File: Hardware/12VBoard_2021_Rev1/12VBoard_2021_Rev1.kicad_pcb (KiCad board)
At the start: 2 copper layers, 101.6 x 101.6 mm, 170 parts, among them Q1 CSD18537NQ5A, Q10 IRLML2060, Q11 IRLML2060, Q12 IRLML2060, Q13 IRLML2060, Q2 CSD18531Q5A, Q3 IRLML2060, Q4 CSD18537NQ5A, Q5 CSD18531Q5A, Q6 CSD18537NQ5A, Q7 CSD18531Q5A, Q8 IRLML2060, Q9 IRLML2060, U1 LT1910, U10 LM5116, U11 INA198, U12 LM5116, U13 INA198, U14 LT1910, U15 LT1910, U16 LT1910, U17 LT1910, U2 INA198, U3 LT1910, U4 LM2576S-12/NOPB, U5 LT1910, U6 LM2576S-12/NOPB, U7 LM5116, U8 INA198, U9 OKI

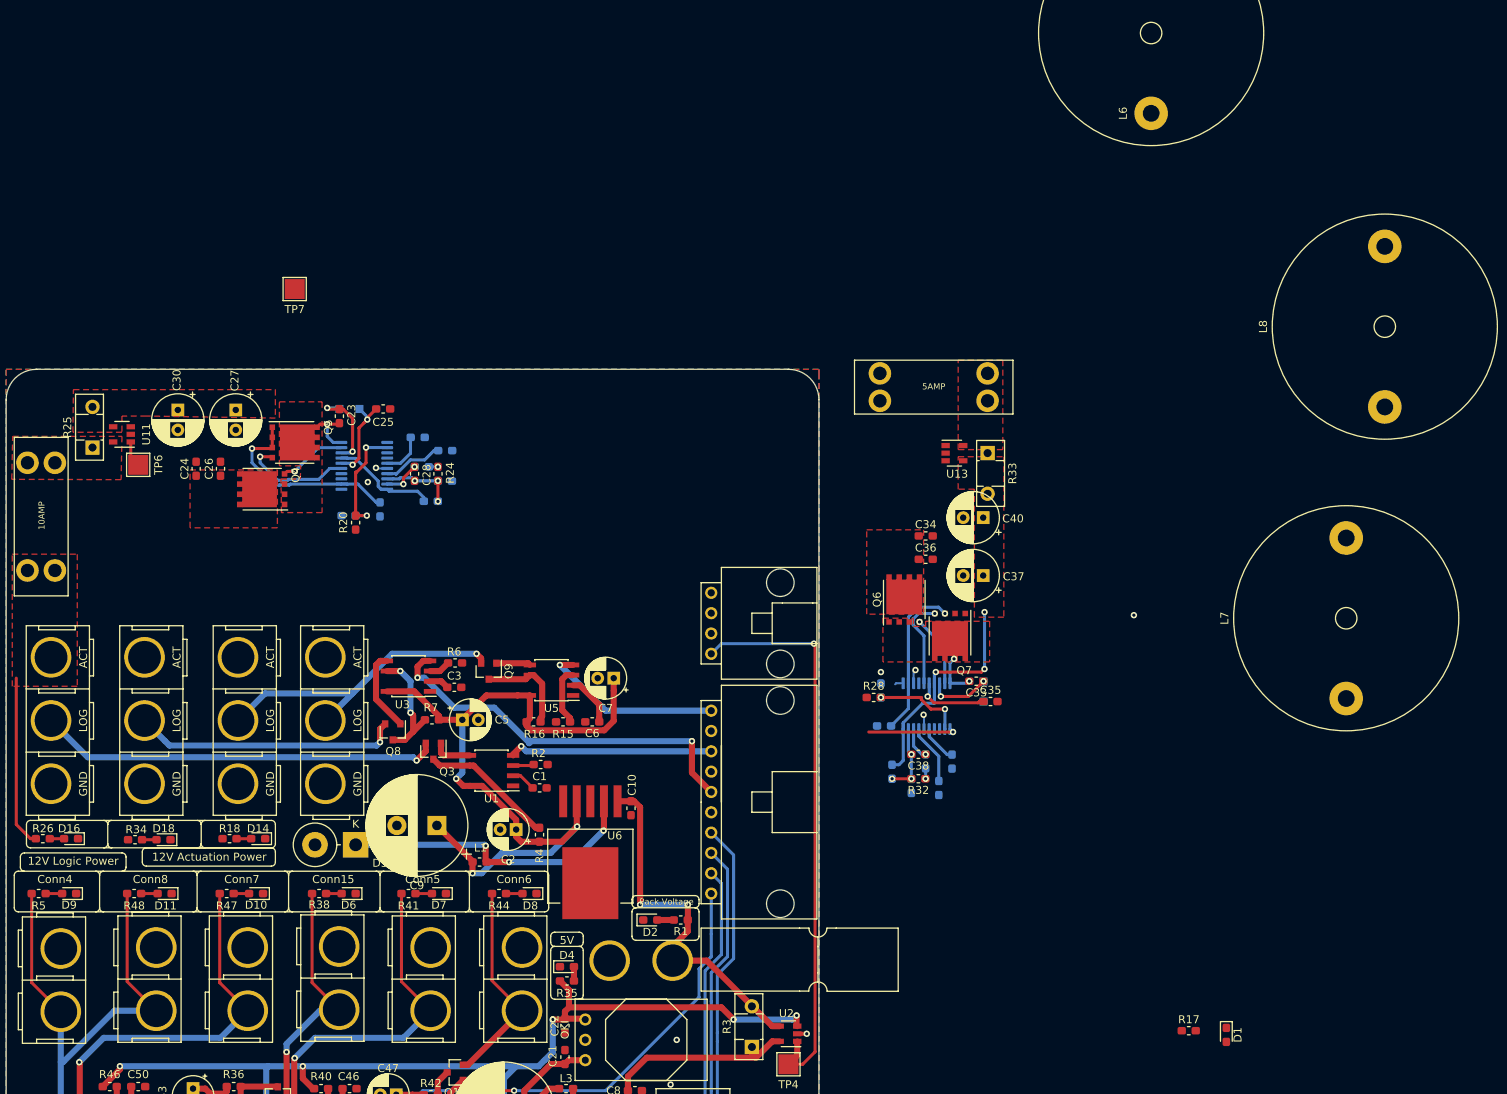
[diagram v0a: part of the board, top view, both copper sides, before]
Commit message: Rearanged logic bick for high current
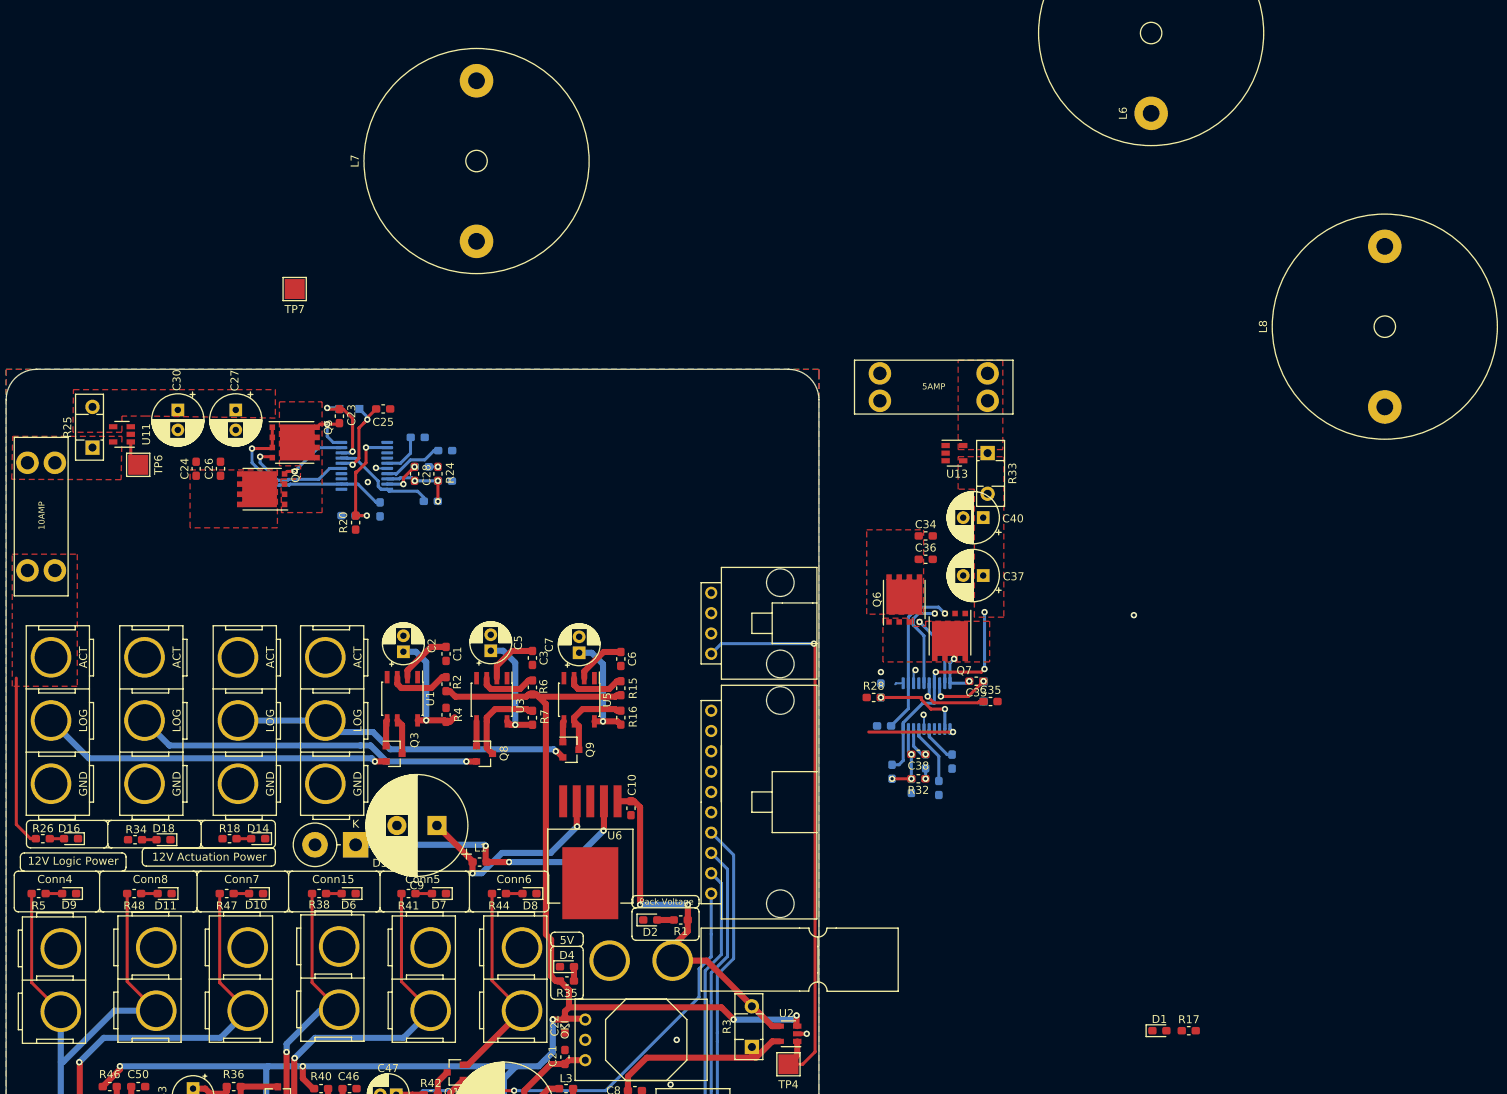
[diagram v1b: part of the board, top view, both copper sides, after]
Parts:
- moved L7 122.8 mm to (174.4, 22.4)
- moved C2 26.3 mm to (165.2, 73.7), turned to 90 degrees
- moved C1 20.4 mm to (170.6, 73.9), turned to 270 degrees
- moved R4 19.0 mm to (170.6, 81.5)
- moved R2 15.5 mm to (170.6, 77.7), turned to 270 degrees
- moved U1 14.3 mm to (165.1, 79.5), turned to 270 degrees
- moved Q9 14.2 mm to (186.2, 85.9), turned to 0 degrees
- moved R7 12.6 mm to (181.4, 81.9), turned to 90 degrees
- moved Q8 11.8 mm to (175.4, 86.4), turned to 0 degrees
- moved R16 10.9 mm to (192.4, 81.9), turned to 90 degrees
- moved U3 10.8 mm to (176.3, 79.7), turned to 270 degrees
- moved C3 10.4 mm to (181.4, 74.4), turned to 270 degrees
- moved R6 10.1 mm to (181.4, 78.1), turned to 270 degrees
- moved C5 9.34 mm to (176.1, 73.5), turned to 90 degrees
- moved C6 8.63 mm to (192.4, 74.6), turned to 270 degrees
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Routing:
- net +5V: track 134.8 -> 194.6 mm
- net /High Current Outputs/GimbalCTL_Log: track 48.5 -> 0.00 mm, vias 2 -> 0
- net /High Current Outputs/AuxMountCTL_Log: track 25.6 -> 0.00 mm, vias 1 -> 0
- net /High Current Outputs/12VLogic/12VLogic: track 97.5 -> 72.2 mm, vias 3 -> 5
- net /High Current Outputs/MultiMediaCTL_Log: track 22.9 -> 0.00 mm, vias 1 -> 0
- net Net-(Q3-Pad3): track 16.8 -> 4.44 mm
- net /High Current Outputs/Gimbal/12VLogicGimbal: track 33.5 -> 43.6 mm
- net Net-(Q8-Pad1): track 10.2 -> 3.11 mm
- net /High Current Outputs/AuxMount/12VLogicAuxMount: track 50.4 -> 44.0 mm
- net Net-(R2-Pad1): track 2.62 -> 7.72 mm
- net Net-(R6-Pad1): track 2.67 -> 7.22 mm
- net Net-(C3-Pad1): track 2.47 -> 6.75 mm
- net Net-(Q8-Pad3): track 15.0 -> 11.1 mm, vias 2 -> 0
- net Net-(C1-Pad1): track 3.07 -> 6.89 mm
- net /High Current Outputs/Multimedia/Extra/12VLogicMultiMedia: track 39.5 -> 43.0 mm
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
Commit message: Extended Board
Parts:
- C24, C26, Q4, Q5, U11: moved to B.Cu
- moved L7 55.3 mm to (139.6, 65.3)
- moved C25 28.7 mm to (191.3, 46.0)
- moved C28 28.7 mm to (195.2, 54.1)
- moved C29 28.7 mm to (196.1, 53.2)
- moved R23 28.7 mm to (199.0, 55.0)
- moved R24 28.7 mm to (198.1, 54.1)
- moved C23 28.7 mm to (185.8, 46.9)
- moved C31 28.7 mm to (195.6, 49.5)
- moved C32 28.7 mm to (199.0, 51.2)
- moved D15 28.7 mm to (187.1, 46.0)
- moved R19 28.7 mm to (190.9, 58.5)
- moved R20 28.7 mm to (187.8, 60.2)
- moved R21 28.7 mm to (186.9, 59.3)
- moved R22 28.7 mm to (197.2, 57.5)
- moved U10 28.7 mm to (188.9, 53.1)
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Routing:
- net /High Current Outputs/12VLogic/12VLogic: track 72.2 -> 107.9 mm
- net CS: track 65.0 -> 48.3 mm, vias 3 -> 2
- net LO: track 37.2 -> 23.2 mm, vias 3 -> 2
- net HO: track 26.3 -> 18.2 mm, vias 3 -> 2
- net SW: track 18.1 -> 12.0 mm, vias 6 -> 5
- net /High Current Outputs/AuxMountSense: track 3.25 -> 0.00 mm
- net HB: track 26.1 -> 22.9 mm, vias 6 -> 5
- net Net-(F2-Pad2): track 0.00 -> 2.52 mm
- net VOUTVCCX: track 49.5 -> 52.0 mm
- added copper zone on B.Cu, net /High Current Outputs/PackVoltage
- added copper zone on B.Cu, net SW
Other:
- board size 101.6 x 101.6 mm -> 101.6 x 129.4 mm

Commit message: I changed stuff
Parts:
- moved C24 25.3 mm to (172.5, 46.7)
- moved C26 25.3 mm to (172.5, 49.8)
- moved Q4 25.3 mm to (175.0, 55.0)
- moved Q5 25.3 mm to (169.2, 59.1)
- moved L7 17.2 mm to (151.4, 52.8), turned to 180 degrees
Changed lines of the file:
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@@
   (page A4)
   (layers
-    (0 F.Cu signal hide)
-    (31 B.Cu signal hide)
+    (0 F.Cu signal)
+    (31 B.Cu signal)
     (32 B.Adhes user)
     (33 F.Adhes user)
@@
   )
   (module Inductor_THT:L_Radial_D27.9mm_P20.07mm_Vishay_IHB-3 (layer F.Cu)
-    (at 139.573 65.278 90)
+    (at 151.384 52.832 180)
     (descr "Inductor, Radial series, Radial, pin pitch=20.07mm, , diameter=27.9mm, Vishay, IHB-3, http://www.vishay.com/docs/34015/ihb.pdf")
     (tags "Inductor Radial series Radial pin pitch 20.07mm  diameter 27.9mm Vishay IHB-3")
-    (fp_text reference L7 (at 10.035 -15.2 90) (layer F.SilkS)
+    (fp_text reference L7 (at 10.035 -15.2) (layer F.SilkS)
       (effects (font (size 1 1) (thickness 0.15)))
     )
-    (fp_text value 10uH (at 10.035 15.2 90) (layer F.Fab)
+    (fp_text value 10uH (at 10.035 15.2) (layer F.Fab)
       (effects (font (size 1 1) (thickness 0.15)))
     )
-    (fp_text user %R (at 10.035 0 90) (layer F.Fab)
+    (fp_text user %R (at 10.035 0) (layer F.Fab)
       (effects (font (size 1 1) (thickness 0.15)))
     )
@@
     (fp_line (start 24.24 14.2) (end 24.24 -14.2) (layer F.CrtYd) (width 0.05))
     (fp_line (start 24.24 -14.2) (end -4.17 -14.2) (layer F.CrtYd) (width 0.05))
-    (pad 2 thru_hole circle (at 20.07 0 90) (size 4.2 4.2) (drill 2.1) (layers *.Cu *.Mask)
+    (pad 2 thru_hole circle (at 20.07 0 180) (size 4.2 4.2) (drill 2.1) (layers *.Cu *.Mask)
       (net 5 VOUTVCCX))
-    (pad 1 thru_hole circle (at 0 0 90) (size 4.2 4.2) (drill 2.1) (layers *.Cu *.Mask)
+    (pad 1 thru_hole circle (at 0 0 180) (size 4.2 4.2) (drill 2.1) (layers *.Cu *.Mask)
       (net 23 SW))
     (model ${KISYS3DMOD}/Inductor_THT.3dshapes/L_Radial_D27.9mm_P20.07mm_Vishay_IHB-3.wrl
@@
   )
   (module Capacitor_SMD:C_0603_1608Metric_Pad1.05x0.95mm_HandSolder (layer B.Cu)
-    (at 147.814 55.372 180)
+    (at 172.452 49.784 180)
     (descr "Capacitor SMD 0603 (1608 Metric), square (rectangular) end terminal, IPC_7351 nominal with elongated pad for handsoldering. (Body size source: http://www.tortai-tech.com/upload/download/2011102023233369053.pdf), generated with kicad-footprint-generator")
     (tags "capacitor handsolder")
@@
   )
   (module Capacitor_SMD:C_0603_1608Metric_Pad1.05x0.95mm_HandSolder (layer B.Cu)
-    (at 147.814 52.324 180)
+    (at 172.452 46.736 180)
     (descr "Capacitor SMD 0603 (1608 Metric), square (rectangular) end terminal, IPC_7351 nominal with elongated pad for handsoldering. (Body size source: http://www.tortai-tech.com/upload/download/2011102023233369053.pdf), generated with kicad-footprint-generator")
     (tags "capacitor handsolder")
@@
   )
   (module Package_SON:VSONP-8-1EP_5x6_P1.27mm (layer B.Cu)
-    (at 150.368 60.579 90)
+    (at 175.006 54.991 90)
     (descr "SON, 8-Leads, Body 5x6x1mm, Pitch 1.27mm; (see Texas Instruments CSD18531Q5A http://www.ti.com/lit/ds/symlink/csd18531q5a.pdf)")
     (tags "VSONP 1.27")
@@
   )
   (module Package_SON:VSONP-8-1EP_5x6_P1.27mm (layer B.Cu)
-    (at 144.526 64.643 270)
+    (at 169.164 59.055 270)
     (descr "SON, 8-Leads, Body 5x6x1mm, Pitch 1.27mm; (see Texas Instruments CSD18531Q5A http://www.ti.com/lit/ds/symlink/csd18531q5a.pdf)")
     (tags "VSONP 1.27")
@@
   (segment (start 352.679 87.376) (end 352.679 84.963) (width 0.381) (layer B.Cu) (net 23))
   (segment (start 352.679 87.376) (end 355.092 87.376) (width 0.381) (layer B.Cu) (net 23))
-  (segment (start 142.24 67.824) (end 142.621 67.443) (width 0.381) (layer B.Cu) (net 23))
+  (segment (start 166.878 62.236) (end 167.259 61.855) (width 0.381) (layer B.Cu) (net 23))
   (via (at 229.743 69.932) (size 0.8) (drill 0.4) (layers F.Cu B.Cu) (net 24))
   (segment (start 232.903 73.092) (end 229.743 69.932) (width 0.381) (layer B.Cu) (net 24))
@@
   (segment (start 352.029 83.252) (end 348.742 79.965) (width 0.381) (layer B.Cu) (net 24))
   (segment (start 352.029 87.376) (end 352.029 83.252) (width 0.381) (layer B.Cu) (net 24))
-  (segment (start 148.1455 63.6965) (end 148.463 63.379) (width 0.381) (layer B.Cu) (net 24))
+  (segment (start 172.7835 58.1085) (end 173.101 57.791) (width 0.381) (layer B.Cu) (net 24))
   (segment (start 188.113 55.365) (end 186.7925 55.365) (width 0.381) (layer B.Cu) (net 25))
   (segment (start 190.406 57.658) (end 188.113 55.365) (width 0.381) (layer B.Cu) (net 25))
@@
   (segment (start 347.479 88.1135) (end 347.479 87.376) (width 0.381) (layer B.Cu) (net 25))
   (segment (start 345.186 92.837) (end 345.186 92.362) (width 0.381) (layer B.Cu) (net 25))
-  (segment (start 142.621 61.843) (end 143.891 61.843) (width 0.381) (layer B.Cu) (net 25))
-  (segment (start 143.891 61.843) (end 145.161 61.843) (width 0.381) (layer B.Cu) (net 25))
+  (segment (start 167.259 56.255) (end 168.529 56.255) (width 0.381) (layer B.Cu) (net 25))
+  (segment (start 168.529 56.255) (end 169.799 56.255) (width 0.381) (layer B.Cu) (net 25))
   (segment (start 229.626058 68.879) (end 231.648 68.879) (width 0.381) (layer B.Cu) (net 26))
   (segment (start 228.952499 69.552559) (end 229.626058 68.879) (width 0.381) (layer B.Cu) (net 26))
@@
     (polygon
       (pts
-        (xy 149.098 65.3415) (xy 147.447 65.405) (xy 147.447 62.738) (xy 136.906 62.738) (xy 136.906 68.072)
-        (xy 153.289 68.072) (xy 153.289 62.992) (xy 149.098 62.9285)
+        (xy 173.736 59.7535) (xy 172.085 59.817) (xy 172.085 57.15) (xy 161.544 57.15) (xy 161.544 62.484)
+        (xy 177.927 62.484) (xy 177.927 57.404) (xy 173.736 57.3405)
       )
     )
@@
     (polygon
       (pts
-        (xy 217.17 38.862) (xy 217.17 139.954) (xy 115.57 139.954) (xy 115.57 38.354) (xy 217.17 38.354)
+        (xy 217.17 38.862) (xy 217.17 139.954) (xy 115.57 139.954) (xy 115.57 10.541) (xy 217.17 10.541)
       )
     )
@@
     (polygon
       (pts
-        (xy 217.17 38.862) (xy 217.17 139.954) (xy 115.57 139.954) (xy 115.57 38.354) (xy 217.17 38.354)
+        (xy 217.17 38.862) (xy 217.17 139.954) (xy 115.57 139.954) (xy 115.57 10.541) (xy 217.17 10.541)
       )
     )
@@
     (polygon
       (pts
-        (xy 147.955 62.484) (xy 155.194 62.484) (xy 155.194 51.562) (xy 147.955 51.562)
+        (xy 172.593 56.896) (xy 179.832 56.896) (xy 179.832 45.974) (xy 172.593 45.974)
       )
     )

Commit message: Started work on updated layout
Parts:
- removed the C14 at (349.4, 69.0)
- removed the C15 at (356.7, 66.7)
- removed the C16 at (355.0, 97.4)
- removed the C18 at (356.7, 73.9)
- removed C19, C31, C41: 470pF, Capacitor_SMD:C_0603_1608Metric_Pad1.05x0.95mm_HandSolder
- removed C20: 33pF, Capacitor_SMD:C_0603_1608Metric_Pad1.05x0.95mm_HandSolder
- removed C23, C26, C33, C36: 100nF, Capacitor_SMD:C_0603_1608Metric_Pad1.05x0.95mm_HandSolder
- removed C24, C34: 2.2uF, Capacitor_SMD:C_0603_1608Metric_Pad1.05x0.95mm_HandSolder
- removed C25, C35: 1uF, Capacitor_SMD:C_0603_1608Metric_Pad1.05x0.95mm_HandSolder
- removed C27, C30, C37, C40: 100uF, Capacitor_THT:CP_Radial_D6.3mm_P2.50mm
- removed C28, C38: 10pF, Capacitor_SMD:C_0603_1608Metric_Pad1.05x0.95mm_HandSolder
- removed C29, C39: 120pF, Capacitor_SMD:C_0603_1608Metric_Pad1.05x0.95mm_HandSolder
- removed C32, C42: 33nF, Capacitor_SMD:C_0603_1608Metric_Pad1.05x0.95mm_HandSolder
- removed the D12 at (356.9, 88.7)
- removed D17: 1.25V 250mA, Diode_SMD:D_SOD-323_HandSoldering
- removed L6, L7, L8: 10uH, Inductor_THT:L_Radial_D27.9mm_P20.07mm_Vishay_IHB-3
- removed Q1, Q4, Q6: CSD18537NQ5A, Package_SON:VSONP-8-1EP_5x6_P1.27mm
- removed Q2, Q5, Q7: CSD18531Q5A, Package_SON:VSONP-8-1EP_5x6_P1.27mm
- removed the R10 at (343.3, 88.5)
- removed R24, R32: 261K, Resistor_SMD:R_0603_1608Metric_Pad1.05x0.95mm_HandSolder
- removed R25: 50m, Package_TO_SOT_THT:TO-126-2_Vertical
- removed R26: 1.2k, Resistor_SMD:R_0603_1608Metric_Pad1.05x0.95mm_HandSolder
- removed R27: 5m, Resistor_SMD:R_0603_1608Metric_Pad1.05x0.95mm_HandSolder
- removed R28: 36.5K, Resistor_SMD:R_0603_1608Metric_Pad1.05x0.95mm_HandSolder
- removed R29: 2.26K, Resistor_SMD:R_0603_1608Metric_Pad1.05x0.95mm_HandSolder
- removed R30: 86.6K, Resistor_SMD:R_0603_1608Metric_Pad1.05x0.95mm_HandSolder
- removed R31: 9.76k, Resistor_SMD:R_0603_1608Metric_Pad1.05x0.95mm_HandSolder
- removed TP6: TestPoint, TestPoint:TestPoint_Pad_2.5x2.5mm
- removed the U10 at (188.9, 53.1)
- removed the U12 at (230.6, 80.5)
- removed the U7 at (349.8, 90.2)
- added C13: 0.1uF, Capacitor_SMD:C_0603_1608Metric_Pad1.05x0.95mm_HandSolder, F.Cu at (252.5, 91.1)
- added C14: 10uF, Capacitor_THT:CP_Radial_D5.0mm_P2.00mm, F.Cu at (257.8, 88.3)
- added C14: 10uF, Capacitor_THT:CP_Radial_D5.0mm_P2.00mm, F.Cu at (349.4, 69.0)
- added C15: 0.1uF, Capacitor_SMD:C_0603_1608Metric_Pad1.05x0.95mm_HandSolder, F.Cu at (283.1, 104.6)
- added C15: 0.1uF, Capacitor_SMD:C_0603_1608Metric_Pad1.05x0.95mm_HandSolder, F.Cu at (356.7, 66.7)
- added C16: 10uF, Capacitor_THT:CP_Radial_D5.0mm_P2.00mm, F.Cu at (283.1, 100.1)
- added C16: 10uF, Capacitor_THT:CP_Radial_D5.0mm_P2.00mm, F.Cu at (354.1, 109.5)
- added C17: 0.1uF, Capacitor_SMD:C_0603_1608Metric_Pad1.05x0.95mm_HandSolder, F.Cu at (289.4, 85.0)
- added C18: 10uF, Capacitor_THT:CP_Radial_D5.0mm_P2.00mm, F.Cu at (289.4, 80.5)
- added C18: 10uF, Capacitor_THT:CP_Radial_D5.0mm_P2.00mm, F.Cu at (356.7, 73.9)
- added D1: Logic Power Green, Diode_SMD:D_0603_1608Metric_Pad1.05x0.95mm_HandSolder, F.Cu at (259.9, 104.9)
- added D12: Aux Mount Acuation Gree, Diode_SMD:D_0603_1608Metric_Pad1.05x0.95mm_HandSolder, F.Cu at (248.1, 91.2)
- added D12: Aux Mount Acuation Gree, Diode_SMD:D_0603_1608Metric_Pad1.05x0.95mm_HandSolder, B.Cu at (362.7, 105.2)
- added D13: Aux Mount Acuation Gree, Diode_SMD:D_0603_1608Metric_Pad1.05x0.95mm_HandSolder, F.Cu at (145.4, -6.75)
- added F4: 5A, MRDT_Passives:ATC_Fuse_Block, F.Cu at (249.6, 79.4)
- added R10: 50m, Package_TO_SOT_THT:TO-126-2_Vertical, F.Cu at (248.1, 87.8)
- added R10: 50m, Package_TO_SOT_THT:TO-126-2_Vertical, B.Cu at (343.3, 116.3)
- added R11: 0.01, Resistor_SMD:R_0603_1608Metric_Pad1.05x0.95mm_HandSolder, F.Cu at (268.8, 89.5)
- added R12: 1.2k, Resistor_SMD:R_0603_1608Metric_Pad1.05x0.95mm_HandSolder, F.Cu at (268.6, 92.0)
- added R13: 5.1K, Resistor_SMD:R_0603_1608Metric_Pad1.05x0.95mm_HandSolder, F.Cu at (278.8, 104.6)
- added R17: 0.01, Resistor_SMD:R_0603_1608Metric_Pad1.05x0.95mm_HandSolder, F.Cu at (274.4, 104.5)
- added R19: 5.1K, Resistor_SMD:R_0603_1608Metric_Pad1.05x0.95mm_HandSolder, F.Cu at (285.0, 85.0)
- added R20: 0.01, Resistor_SMD:R_0603_1608Metric_Pad1.05x0.95mm_HandSolder, F.Cu at (280.7, 84.9)
- added R8: 1.2k, Resistor_SMD:R_0603_1608Metric_Pad1.05x0.95mm_HandSolder, F.Cu at (264.3, 104.8)
- added R9: 5.1K, Resistor_SMD:R_0603_1608Metric_Pad1.05x0.95mm_HandSolder, F.Cu at (264.2, 90.9)
- added TP1: TestPoint, TestPoint:TestPoint_Pad_2.5x2.5mm, F.Cu at (264.3, 87.3)
- added U10: INA198, Package_TO_SOT_SMD:SOT-23-5, F.Cu at (269.3, 86.0)
- added U10: INA198, Package_TO_SOT_SMD:SOT-23-5, B.Cu at (192.5, 65.5)
- added U12: LT1910, Package_SO:SOIC-8-N7_3.9x4.9mm_P1.27mm, F.Cu at (276.5, 100.1)
- added U12: LT1910, Package_SO:SOIC-8-N7_3.9x4.9mm_P1.27mm, B.Cu at (235.7, 98.0)
- added U18: FDS66900AS, Package_SO:SOIC-8_3.9x4.9mm_P1.27mm, F.Cu at (205.3, -47.1)
- added U19: LT1910, Package_SO:SOIC-8-N7_3.9x4.9mm_P1.27mm, F.Cu at (282.8, 80.4)
- added U20: FDS66900AS, Package_SO:SOIC-8_3.9x4.9mm_P1.27mm, F.Cu at (132.5, -4.82)
- added U7: LT1910, Package_SO:SOIC-8-N7_3.9x4.9mm_P1.27mm, F.Cu at (271.1, 80.4)
- added U7: LT1910, Package_SO:SOIC-8-N7_3.9x4.9mm_P1.27mm, B.Cu at (348.0, 109.7)
- added VR1: Q36SR12020NRFA, MRDT_Actives:Q36SR12020NRFA, F.Cu at (160.5, -21.6)
- C10: value 100uF -> 330uF; footprint Capacitor_SMD:C_0603_1608Metric_Pad1.05x0.95mm_HandSolder -> Capacitor_THT:CP_Radial_D8.0mm_P3.50mm
- C11: value 2.2uF -> 330uF; footprint Capacitor_SMD:C_0603_1608Metric_Pad1.05x0.95mm_HandSolder -> Capacitor_THT:CP_Radial_D8.0mm_P3.50mm
- C13: value 1uF -> 0.1uF
- C17: value 120pF -> 0.1uF
- C4, C9: footprint Capacitor_THT:CP_Radial_D12.5mm_P5.00mm -> Capacitor_THT:CP_Radial_D10.0mm_P5.00mm
- D14: value Multimedia Acuation Green -> Multimedia Actuation Green
- D15: value 1.25V 250mA -> Aux Mount Acuation Gree; footprint Diode_SMD:D_SOD-323_HandSoldering -> Diode_SMD:D_0603_1608Metric_Pad1.05x0.95mm_HandSolder
- D16: value AuxMount Acuation Green -> Aux Mount Acuation Gree
- F1: value 10AMP -> 10A
- F2: value 10AMP -> 20
- F3: value 5AMP -> 5A
- R11: value 86.6K -> 0.01
- R12: value 9.76 -> 1.2k
- R13: value 261K -> 5.1K
- R17: value 1.2k -> 0.01
- R19: value 5m -> 5.1K
- R20: value 36.5K -> 0.01
- R21: value 2.26K -> 1.2k
- R22: value 86.6K -> 1.2k
- R23: value 9.76K -> 1.2k
- R8: value 5m -> 1.2k
- R9: value 36.5K -> 5.1K
- U11: value INA198 -> FDS66900AS; footprint Package_TO_SOT_SMD:SOT-23-5 -> Package_SO:SOIC-8_3.9x4.9mm_P1.27mm
- moved C12 162.5 mm to (193.5, 93.2), turned to 270 degrees
- moved C10 76.0 mm to (255.5, 49.0)
- moved TP7 52.2 mm to (114.0, -7.87)
- moved R13 23.8 mm to (365.5, 120.1)
- moved R12 19.8 mm to (369.5, 115.3)
- moved C11 19.2 mm to (368.3, 75.2)
- moved C13 18.3 mm to (365.6, 106.4)
- moved R9 17.0 mm to (341.6, 106.4)
- moved R8 16.6 mm to (338.6, 108.5)
- moved R11 14.6 mm to (363.0, 114.6)
- moved C17 13.7 mm to (361.7, 109.0)
- moved D15 11.9 mm to (178.6, 54.4)
- moved U11 10.4 mm to (130.6, 42.7)
- moved R23 6.49 mm to (199.4, 61.5)
- moved R22 5.93 mm to (195.7, 63.2)
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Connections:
- C1 pad 2: AGNDPGND -> GND
- C10 pad 1: /High Current Outputs/PackVoltage -> Net-(C10-Pad1)
- C10 pad 2: AGNDPGND -> GND
- C11 pad 1: /High Current Outputs/PackVoltage -> /High Current Outputs/12VActuation
- C11 pad 2: AGNDPGND -> GND
- C12 pad 1: HB -> /High Current Outputs/PackVoltage
- C12 pad 2: SW -> GND
- C13 pad 1: VCC -> Net-(C13-Pad1)
- C13 pad 2: AGNDPGND -> GND
- C17 pad 2: Net-(C17-Pad2) -> GND
- C2 pad 1: /High Current Outputs/12VLogic/12VLogic -> /High Current Outputs/12VLogic
- C2 pad 2: AGNDPGND -> GND
- C21 pad 2: AGNDPGND -> GND
- C22 pad 2: AGNDPGND -> GND
- C3 pad 2: AGNDPGND -> GND
- C4 pad 2: AGNDPGND -> GND
- C43 pad 2: AGNDPGND -> GND
- C44 pad 2: AGNDPGND -> GND
- C45 pad 2: AGNDPGND -> GND
- C46 pad 2: AGNDPGND -> GND
- C47 pad 2: AGNDPGND -> GND
- C48 pad 2: AGNDPGND -> GND
- C49 pad 2: AGNDPGND -> GND
- C5 pad 1: /High Current Outputs/12VLogic/12VLogic -> /High Current Outputs/12VLogic
- C5 pad 2: AGNDPGND -> GND
- C50 pad 2: AGNDPGND -> GND
- C6 pad 2: AGNDPGND -> GND
- C7 pad 1: /High Current Outputs/12VLogic/12VLogic -> /High Current Outputs/12VLogic
- C7 pad 2: AGNDPGND -> GND
- C8 pad 2: AGNDPGND -> GND
- C9 pad 1: /High Current Outputs/12VLogic/12VLogic -> /High Current Outputs/12VLogic
- C9 pad 2: AGNDPGND -> GND
- Conn1 pad 2: /Tiva In/Outputs/MultimediaCTL_Act -> /High Current Outputs/MultimediaCTL_Act
- Conn10 pad 1: AGNDPGND -> GND
- Conn11 pad 1: AGNDPGND -> GND
- Conn11 pad 3: /High Current Outputs/Multimedia/Extra/12V10AMultiMedia -> Net-(Conn11-Pad3)
- Conn12 pad 1: AGNDPGND -> GND
- Conn12 pad 3: /High Current Outputs/Multimedia/Extra/12V10AMultiMedia -> Net-(Conn11-Pad3)
- Conn15 pad 1: AGNDPGND -> GND
- Conn2 pad 1: /Tiva In/Outputs/MultimediaSense -> /High Current Outputs/MultimediaSense
- Conn3 pad 1: AGNDPGND -> GND
- Conn4 pad 1: AGNDPGND -> GND
- Conn5 pad 1: AGNDPGND -> GND
- Conn6 pad 1: AGNDPGND -> GND
- Conn7 pad 1: AGNDPGND -> GND
- Conn8 pad 1: AGNDPGND -> GND
- Conn9 pad 1: AGNDPGND -> GND
- D1 pad 1: AGNDPGND -> GND
- D10 pad 1: AGNDPGND -> GND
- D11 pad 1: AGNDPGND -> GND
- D14 pad 1: AGNDPGND -> GND
- D15 pad 1: HB -> GND
- D15 pad 2: VCC -> Net-(D15-Pad2)
- D16 pad 1: AGNDPGND -> GND
- D18 pad 1: AGNDPGND -> GND
- D2 pad 1: AGNDPGND -> GND
- D3 pad 2: AGNDPGND -> GND
- D4 pad 1: AGNDPGND -> GND
- D5 pad 2: AGNDPGND -> GND
- D6 pad 1: AGNDPGND -> GND
- D7 pad 1: AGNDPGND -> GND
- D8 pad 1: AGNDPGND -> GND
- D9 pad 1: AGNDPGND -> GND
- F1 pad 1: /High Current Outputs/Multimedia/Extra/12V10AMultiMedia -> /High Current Outputs/Multimedia/Extra/12V5AON
- F2 pad 1: /High Current Outputs/AuxMount/12V10AAuxMount -> Net-(C10-Pad1)
- F2 pad 2: Net-(F2-Pad2) -> /High Current Outputs/12VActuation
- F3 pad 1: /High Current Outputs/Gimbal/12V5AGimbal -> /High Current Outputs/Gimbal/12V5AON
- L1 pad 2: /High Current Outputs/12VLogic/12VLogic -> /High Current Outputs/12VLogic
- R11 pad 1: VOUTVCCX -> /High Current Outputs/AuxMount/12V5AON
- R11 pad 2: COMPFB -> Net-(R11-Pad2)
- R12 pad 1: COMPFB -> /High Current Outputs/AuxMount/12V10AAuxMount
- R12 pad 2: AGNDPGND -> Net-(D12-Pad2)
- R13 pad 1: Net-(C17-Pad2) -> Net-(R13-Pad1)
- R13 pad 2: COMPFB -> +5V
- R14 pad 2: VOUTVCCX -> /High Current Outputs/Multimedia/Extra/12Actuation
- R16 pad 1: /High Current Outputs/12VLogic/12VLogic -> /High Current Outputs/12VLogic
- R17 pad 1: /High Current Outputs/12VLogic/12VLogic -> /High Current Outputs/Gimbal/12V5AON
- R17 pad 2: Net-(D1-Pad2) -> Net-(R17-Pad2)
- R18 pad 1: /High Current Outputs/Multimedia/Extra/12V10AMultiMedia -> /High Current Outputs/Multimedia/Extra/12V5AMultimedia
- R19 pad 1: CS -> Net-(R19-Pad1)
- R19 pad 2: AGNDPGND -> +5V
- R20 pad 1: /High Current Outputs/PackVoltage -> /High Current Outputs/Multimedia/Extra/12V5AON
- R21 pad 1: Net-(R20-Pad2) -> /High Current Outputs/AuxMount/12VLogicAuxMount
- R21 pad 2: AGNDPGND -> Net-(D13-Pad2)
- R22 pad 1: VOUTVCCX -> /High Current Outputs/Gimbal/12VLogicGimbal
- R22 pad 2: COMPFB -> Net-(D15-Pad2)
- R23 pad 1: COMPFB -> /High Current Outputs/Multimedia/Extra/12VLogicMultiMedia
- R23 pad 2: AGNDPGND -> Net-(D16-Pad2)
- R33 pad 2: VOUTVCCX -> /High Current Outputs/Gimbal/12Actuation
- R4 pad 1: /High Current Outputs/12VLogic/12VLogic -> /High Current Outputs/12VLogic
- R7 pad 1: /High Current Outputs/12VLogic/12VLogic -> /High Current Outputs/12VLogic
- R8 pad 1: CS -> /High Current Outputs/12VLogic
- R8 pad 2: AGNDPGND -> Net-(D1-Pad2)
- R9 pad 1: /High Current Outputs/PackVoltage -> Net-(R9-Pad1)
- R9 pad 2: Net-(R10-Pad1) -> +5V
- TP5 pad 1: /High Current Outputs/Multimedia/Extra/MultimediaExtraSense -> /High Current Outputs/MultimediaSense
- U1 pad 1: AGNDPGND -> GND
- U1 pad 8: /High Current Outputs/12VLogic/12VLogic -> /High Current Outputs/12VLogic
- U11 pad 1: /High Current Outputs/AuxMountSense -> Net-(R11-Pad2)
- U11 pad 2: AGNDPGND -> Net-(R11-Pad2)
- U11 pad 3: +5V -> Net-(R11-Pad2)
- U11 pad 4: VOUTVCCX -> Net-(U11-Pad4)
- U11 pad 5: Net-(F2-Pad2) -> /High Current Outputs/AuxMount/12V10AAuxMount
- U13 pad 2: AGNDPGND -> GND
- U13 pad 4: VOUTVCCX -> /High Current Outputs/Gimbal/12Actuation
- U14 pad 1: AGNDPGND -> GND
- U15 pad 1: AGNDPGND -> GND
- U16 pad 1: AGNDPGND -> GND
- U17 pad 1: AGNDPGND -> GND
- U2 pad 2: AGNDPGND -> GND
- U3 pad 1: AGNDPGND -> GND
- U3 pad 8: /High Current Outputs/12VLogic/12VLogic -> /High Current Outputs/12VLogic
- U4 pad 3: AGNDPGND -> GND
- U4 pad 5: AGNDPGND -> GND
- U4 pad 6: AGNDPGND -> GND
- U5 pad 1: AGNDPGND -> GND
- U5 pad 8: /High Current Outputs/12VLogic/12VLogic -> /High Current Outputs/12VLogic
- U6 pad 3: AGNDPGND -> GND
- U6 pad 4: /High Current Outputs/12VLogic/12VLogic -> /High Current Outputs/12VLogic
- U6 pad 5: AGNDPGND -> GND
- U6 pad 6: AGNDPGND -> GND
- U8 pad 1: /High Current Outputs/Multimedia/Extra/MultimediaExtraSense -> /High Current Outputs/MultimediaSense
- U8 pad 2: AGNDPGND -> GND
- U8 pad 4: VOUTVCCX -> /High Current Outputs/Multimedia/Extra/12Actuation
- U9 pad 2: AGNDPGND -> GND
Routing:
- net /High Current Outputs/12VLogic/12VLogic: track 107.9 -> 0.00 mm, vias 5 -> 0
- net /High Current Outputs/12VLogic: track 0.00 -> 107.9 mm, vias 0 -> 5
- net VOUTVCCX: track 52.0 -> 0.00 mm, vias 3 -> 0
- net CS: track 48.3 -> 0.00 mm, vias 2 -> 0
- net /High Current Outputs/PackVoltage: track 69.0 -> 27.5 mm, vias 4 -> 1
- net COMPFB: track 33.9 -> 0.00 mm, vias 7 -> 0
- net VCC: track 29.7 -> 0.00 mm, vias 5 -> 0
- net LO: track 23.2 -> 0.00 mm, vias 2 -> 0
- net HB: track 22.9 -> 0.00 mm, vias 5 -> 0
- net /High Current Outputs/MultiMediaCTL_Act: track 22.9 -> 0.00 mm, vias 1 -> 0
- net /High Current Outputs/AuxMount/12V10AAuxMount: track 21.5 -> 0.00 mm
- net HO: track 18.2 -> 0.00 mm, vias 2 -> 0
- net Net-(R20-Pad2): track 14.6 -> 0.00 mm, vias 2 -> 0
- net Net-(C20-Pad1): track 13.6 -> 0.00 mm, vias 1 -> 0
- net AGNDPGND: track 12.8 -> 0.00 mm, vias 16 -> 0
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- added copper zone on B.Cu, net GND
- added copper zone on F.Cu, net GND
- removed copper zone on F.Cu, net /High Current Outputs/AuxMount/12V10AAuxMount
- removed copper zone on F.Cu, net /High Current Outputs/PackVoltage
- removed copper zone on B.Cu, net AGNDPGND
- removed copper zone on F.Cu, net AGNDPGND
- removed copper zone on F.Cu, net Net-(F2-Pad2)
- removed copper zone on F.Cu, net Net-(F3-Pad2)
- removed copper zone on B.Cu, net SW
- removed copper zone on F.Cu, net SW
- removed copper zone on F.Cu, net VOUTVCCX
